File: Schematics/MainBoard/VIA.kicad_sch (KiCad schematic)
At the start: 6 parts, among them IC3 W65C22S6TQG-14, J11 Conn_02x04_Odd_Even, J12 Conn_02x06_Odd_Even, J13 Conn_02x06_Odd_Even

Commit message: Work on PCB
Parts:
- removed D16: 1N4148, Diode_THT:D_DO-35_SOD27_P7.62mm_Horizontal, symbol Diode:1N4148
- removed J11: Conn_02x04_Odd_Even, Connector_PinSocket_2.54mm:PinSocket_2x04_P2.54mm_Horizontal, symbol Connector_Generic:Conn_02x04_Odd_Even
- added D16: 1N4148W, Diode_SMD:D_SOD-123, symbol Diode:1N4148W
- added J9: Conn_02x02_Odd_Even, Connector_PinHeader_1.27mm:PinHeader_2x02_P1.27mm_Vertical_SMD, symbol Connector_Generic:Conn_02x02_Odd_Even
- C47: footprint Capacitor_SMD:C_0603_1608Metric -> Capacitor_SMD:C_0402_1005Metric
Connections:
- net VA_CA1: now also J9.1 (Pin_1)
- net VA_CA2: now also J9.3 (Pin_3)
- net VA_CB1: now also J9.2 (Pin_2)
- net VA_CB2: now also J9.4 (Pin_4)
- net nIRQ: now also D16.2 (A)
- net at IC3.17 (IRQB): now also D16.1 (K)

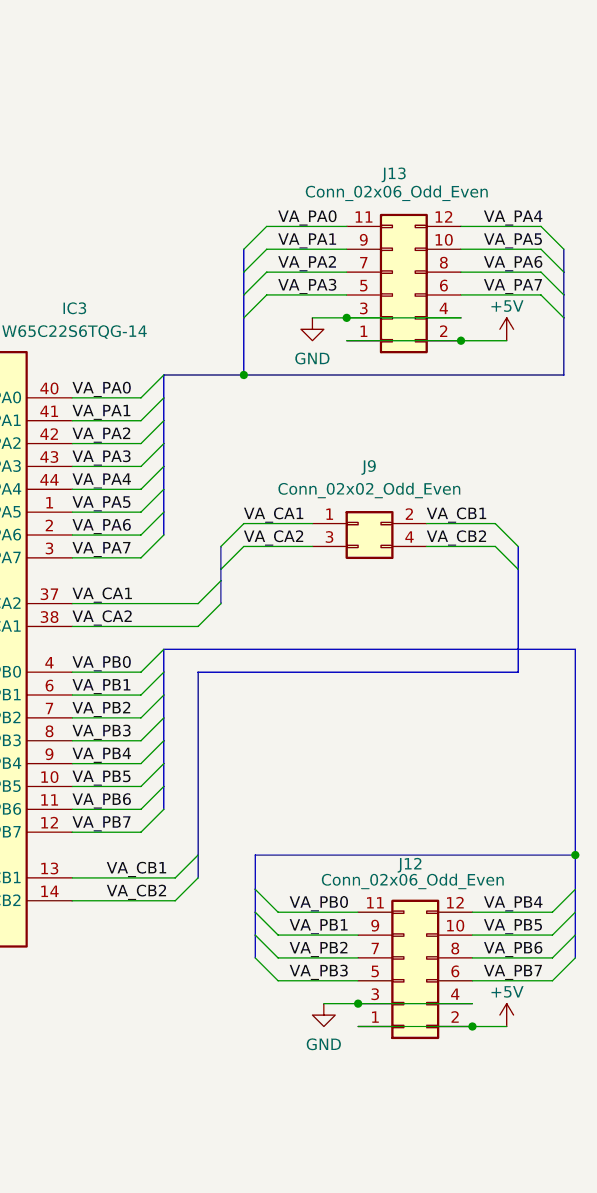
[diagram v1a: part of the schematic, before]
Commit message: Completed routing
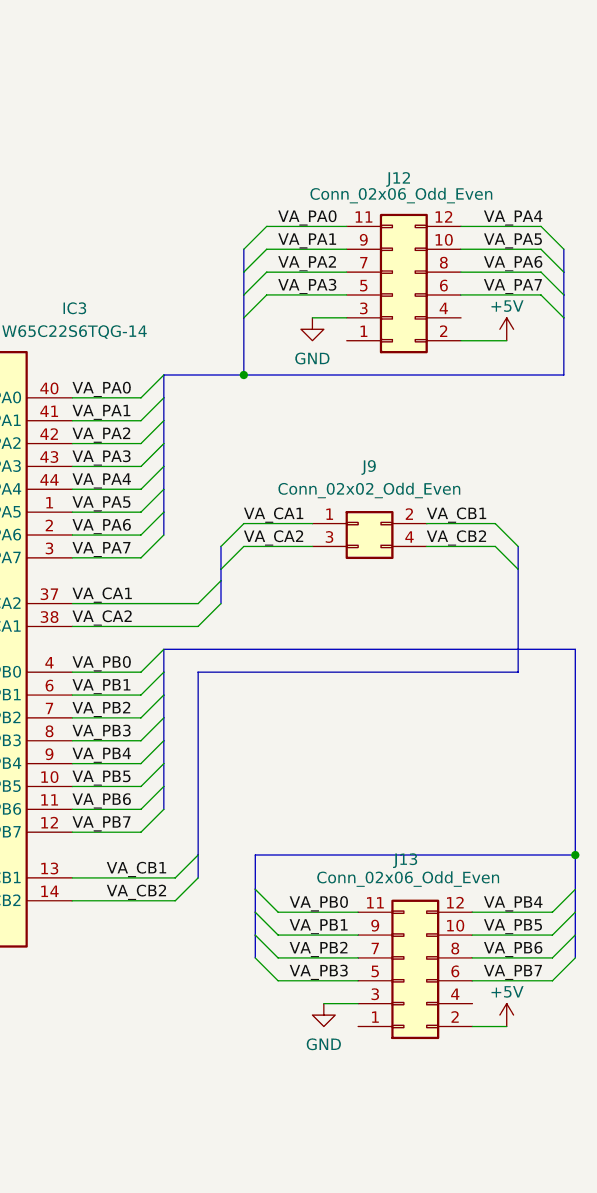
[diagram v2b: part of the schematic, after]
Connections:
- net +5V: no longer J12.1 (Pin_1), J13.1 (Pin_1)
- net GND: no longer J12.4 (Pin_4), J13.4 (Pin_4)
- net VA_PA0: now also J12.11 (Pin_11); no longer J13.11 (Pin_11)
- net VA_PA1: now also J12.9 (Pin_9); no longer J13.9 (Pin_9)
- net VA_PA2: now also J12.7 (Pin_7); no longer J13.7 (Pin_7)
- net VA_PA3: now also J12.5 (Pin_5); no longer J13.5 (Pin_5)
- net VA_PA4: now also J12.12 (Pin_12); no longer J13.12 (Pin_12)
- net VA_PA5: now also J12.10 (Pin_10); no longer J13.10 (Pin_10)
- net VA_PA6: now also J12.8 (Pin_8); no longer J13.8 (Pin_8)
- net VA_PA7: now also J12.6 (Pin_6); no longer J13.6 (Pin_6)
- net VA_PB0: now also J13.11 (Pin_11); no longer J12.11 (Pin_11)
- net VA_PB1: now also J13.9 (Pin_9); no longer J12.9 (Pin_9)
- net VA_PB2: now also J13.7 (Pin_7); no longer J12.7 (Pin_7)
- net VA_PB3: now also J13.5 (Pin_5); no longer J12.5 (Pin_5)
- net VA_PB4: now also J13.12 (Pin_12); no longer J12.12 (Pin_12)
- net VA_PB5: now also J13.10 (Pin_10); no longer J12.10 (Pin_10)
- net VA_PB6: now also J13.8 (Pin_8); no longer J12.8 (Pin_8)
- net VA_PB7: now also J13.6 (Pin_6); no longer J12.6 (Pin_6)
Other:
- moved on the sheet: J12, J13
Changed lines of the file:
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@@
 	(paper "A4")
 	(junction
-		(at 205.74 148.59)
-		(diameter 0)
-		(color 0 0 0 0)
-	)
-	(junction
-		(at 193.04 146.05)
-		(diameter 0)
-		(color 0 0 0 0)
-	)
-	(junction
-		(at 191.77 69.85)
-		(diameter 0)
-		(color 0 0 0 0)
-	)
-	(junction
 		(at 180.34 76.2)
 		(diameter 0)
@@
 		(color 0 0 0 0)
 	)
-	(junction
-		(at 204.47 72.39)
-		(diameter 0)
-		(color 0 0 0 0)
-	)
 	(bus_entry
 		(at 214.63 138.43)
@@
 	(wire
 		(pts
-			(xy 191.77 69.85) (xy 204.47 69.85)
-		)
-		(stroke
-			(width 0)
-			(type default)
-		)
-	)
-	(wire
-		(pts
 			(xy 104.14 99.06) (xy 135.89 99.06)
 		)
@@
 	(wire
 		(pts
-			(xy 204.47 72.39) (xy 209.55 72.39)
-		)
-		(stroke
-			(width 0)
-			(type default)
-		)
-	)
-	(wire
-		(pts
 			(xy 92.71 116.84) (xy 135.89 116.84)
 		)
@@
 	(wire
 		(pts
-			(xy 193.04 148.59) (xy 205.74 148.59)
+			(xy 205.74 148.59) (xy 209.55 148.59)
 		)
 		(stroke
@@
 	(wire
 		(pts
-			(xy 191.77 72.39) (xy 204.47 72.39)
+			(xy 204.47 72.39) (xy 209.55 72.39)
 		)
 		(stroke
@@
 		)
 	)
-	(wire
-		(pts
-			(xy 193.04 146.05) (xy 205.74 146.05)
-		)
-		(stroke
-			(width 0)
-			(type default)
-		)
-	)
 	(bus
 		(pts
@@
 	(wire
 		(pts
-			(xy 205.74 148.59) (xy 209.55 148.59)
-		)
-		(stroke
-			(width 0)
-			(type default)
-		)
-	)
-	(wire
-		(pts
 			(xy 204.47 62.23) (xy 213.36 62.23)
 		)
@@
 	(symbol
 		(lib_id "Connector_Generic:Conn_02x06_Odd_Even")
-		(at 198.12 143.51 0)
+		(at 196.85 67.31 0)
 		(mirror x)
 		(unit 1)
@@
 		(dnp no)
 		(property "Reference" "J12"
-			(at 198.882 130.556 0)
+			(at 197.612 54.356 0)
 			(effects
 				(font
@@
 		)
 		(property "Value" "Conn_02x06_Odd_Even"
-			(at 199.136 132.334 0)
+			(at 197.866 56.134 0)
 			(effects
 				(font
@@
 		)
 		(property "Footprint" "Connector_PinSocket_2.54mm:PinSocket_2x06_P2.54mm_Horizontal"
-			(at 198.12 143.51 0)
+			(at 196.85 67.31 0)
 			(effects
 				(font
@@
 		)
 		(property "Datasheet" "~"
-			(at 198.12 143.51 0)
+			(at 196.85 67.31 0)
 			(effects
 				(font
@@
 		)
 		(property "Description" "Generic connector, double row, 02x06, odd/even pin numbering scheme (row 1 odd numbers, row 2 even numbers), script generated (kicad-library-utils/schlib/autogen/connector/)"
-			(at 198.12 143.51 0)
+			(at 196.85 67.31 0)
 			(effects
 				(font
@@
 		)
 		(property "LCSC" "DNF"
-			(at 198.12 143.51 0)
+			(at 196.85 67.31 0)
 			(effects
 				(font
@@
 	(symbol
 		(lib_id "Connector_Generic:Conn_02x06_Odd_Even")
-		(at 196.85 67.31 0)
+		(at 198.12 143.51 0)
 		(mirror x)
 		(unit 1)
@@
 		(dnp no)
 		(property "Reference" "J13"
-			(at 197.104 53.848 0)
+			(at 198.374 130.048 0)
 			(effects
 				(font
@@
 		)
 		(property "Value" "Conn_02x06_Odd_Even"
-			(at 197.358 55.88 0)
+			(at 198.628 132.08 0)
 			(effects
 				(font
@@
 		)
 		(property "Footprint" "Connector_PinSocket_2.54mm:PinSocket_2x06_P2.54mm_Horizontal"
-			(at 196.85 67.31 0)
+			(at 198.12 143.51 0)
 			(effects
 				(font
@@
 		)
 		(property "Datasheet" "~"
-			(at 196.85 67.31 0)
+			(at 198.12 143.51 0)
 			(effects
 				(font
@@
 		)
 		(property "Description" "Generic connector, double row, 02x06, odd/even pin numbering scheme (row 1 odd numbers, row 2 even numbers), script generated (kicad-library-utils/schlib/autogen/connector/)"
-			(at 196.85 67.31 0)
+			(at 198.12 143.51 0)
 			(effects
 				(font
@@
 		)
 		(property "LCSC" "DNF"
-			(at 196.85 67.31 0)
+			(at 198.12 143.51 0)
 			(effects
 				(font

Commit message: Updates based on production files for JLC
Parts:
- C47: LCSC C113803 -> C307331
- IC3, J12, J13: now not fitted
- J9: LCSC (none) -> DNF; now not fitted
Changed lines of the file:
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@@
 		(in_bom yes)
 		(on_board yes)
-		(dnp no)
+		(dnp yes)
 		(property "Reference" "J12"
 			(at 197.612 54.356 0)
@@
 		(in_bom yes)
 		(on_board yes)
-		(dnp no)
+		(dnp yes)
 		(fields_autoplaced yes)
 		(property "Reference" "J9"
@@
 		)
 		(property "Description" "Generic connector, double row, 02x02, odd/even pin numbering scheme (row 1 odd numbers, row 2 even numbers), script generated (kicad-library-utils/schlib/autogen/connector/)"
+			(at 193.04 92.71 0)
+			(effects
+				(font
+					(size 1.27 1.27)
+				)
+				(hide yes)
+			)
+		)
+		(property "LCSC" "DNF"
 			(at 193.04 92.71 0)
 			(effects
@@
 		(in_bom yes)
 		(on_board yes)
-		(dnp no)
+		(dnp yes)
 		(fields_autoplaced yes)
 		(property "Reference" "IC3"
@@
 		(in_bom yes)
 		(on_board yes)
-		(dnp no)
+		(dnp yes)
 		(property "Reference" "J13"
 			(at 198.374 130.048 0)
@@
 			)
 		)
-		(property "LCSC" "C113803"
+		(property "LCSC" "C307331"
 			(at 129.54 171.45 0)
 			(effects
